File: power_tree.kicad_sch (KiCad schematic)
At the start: 4 parts, among them U3 LM1117MP-3.3

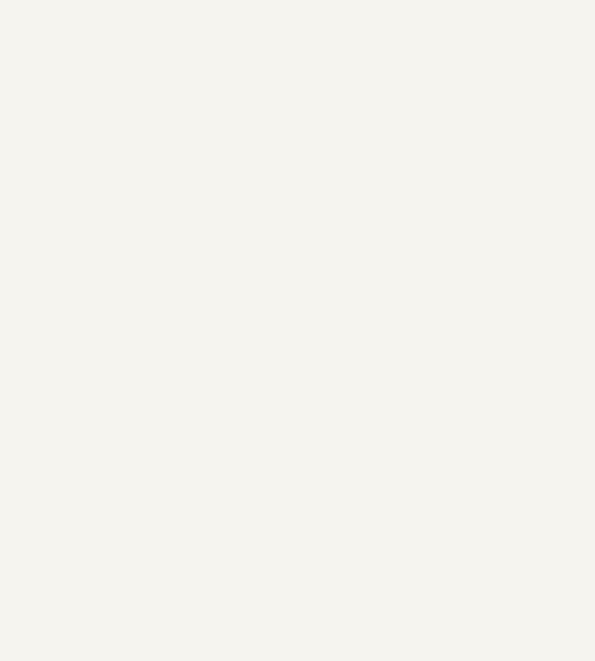
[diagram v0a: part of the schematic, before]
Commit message: feat(connector): Added USB Type-C connector for power input
This commit introduces a USB Type-C connector to the design. This connector will
serve as the primary power input for the board.

The addition of a USB Type-C connector provides a modern and versatile power
interface, offering advantages such as reversible plug orientation and the
potential for higher power delivery in the future. A separate connector
specifically for power input has also been added to provide an alternative or
dedicated power supply option.
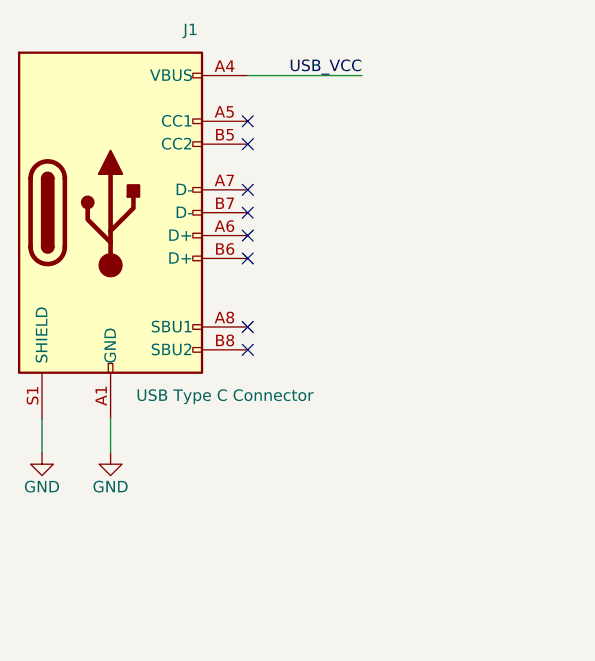
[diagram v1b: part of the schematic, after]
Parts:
- added J1: USB Type C Connector, symbol Connector:USB_C_Receptacle_USB2.0_16P
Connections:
- net GND: now also J1.A1 (GND), J1.A12 (GND), J1.B1 (GND), J1.B12 (GND), J1.S1 (SHIELD)
- net USB_VCC: now also J1.A4 (VBUS), J1.A9 (VBUS), J1.B4 (VBUS), J1.B9 (VBUS)
- no-connect marks 0 -> 8

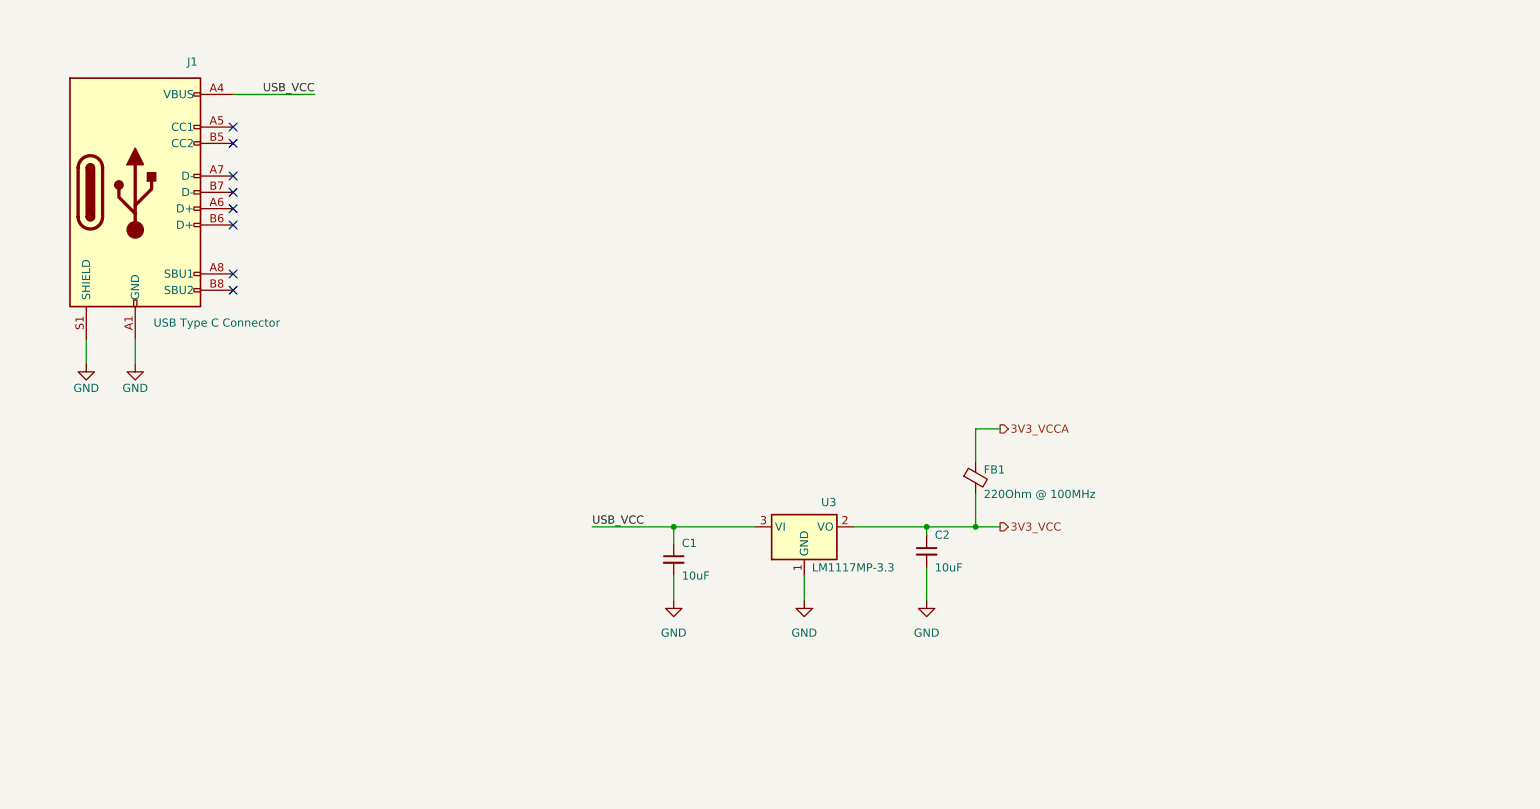
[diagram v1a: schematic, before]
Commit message: feat(usb-uart): add FT232RL USB‑UART bridge and wire RX/TX to MCU
Added the FT232RL USB‑to‑UART interface IC (FT232RL) into the schematic and powered it from the 3.3 V and 5 V rails. Exposed its TTL-level RXD and TXD pins through the hierarchical sheet and connected it to the MCU

- Placed FT232RL SSOP‑28 symbol and footprint, tied VCCIO to 3.3 V, VCC to USB_VCC, and GND to ground.
- Left legacy RS‑232 control lines (DSR#, DCD#, RI#) and CBUS pins unconnected.
- Updated hierarchy:added sheet pins on USB_UART page.

This enables USB‑serial communication between host PC and STM32F030F4Px
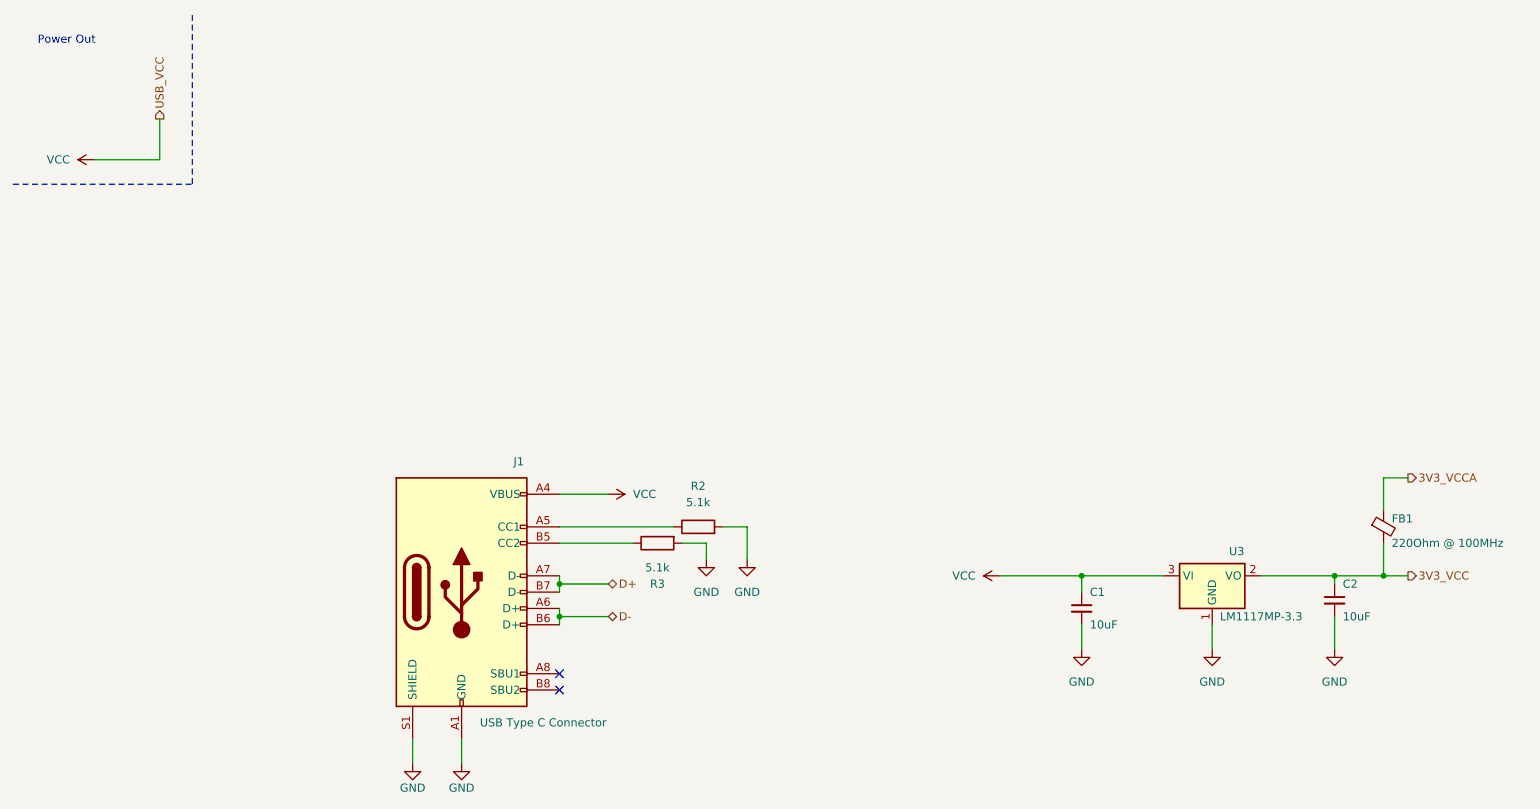
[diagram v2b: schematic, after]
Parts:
- added R2, R3: 5.1k, symbol Device:R
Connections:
- net GND: now also R2.2, R3.2
- net at J1.A5 (CC1): now also R2.1
- net D-: now reaches J1.A6 (D+)
- net D-: now also J1.B6 (D+)
- net D+: now reaches J1.A7 (D-)
- net D+: now also J1.B7 (D-)
- net at J1.B5 (CC2): now also R3.1
- net USB_VCC renamed VCC
- no-connect marks 8 -> 2
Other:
- note added: "Power Out"
- moved on the sheet: C1, C2, FB1, J1, U3

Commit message: feat(usb-uart): add FT232RL for USB-serial, update schematic and layout
Added FT232RL USB‑to‑UART interface IC, powered from 3.3 V and 5 V rails. Connected RXD and TXD to MCU via hierarchical sheet. Left RS‑232 control lines and CBUS pins unconnected. Updated hierarchy with USB_UART sheet pins.

BREAKING CHANGE: USB connector moved to USB_UART sheet; schematic wiring changed to bus-based layout. AGND now kept in separate plane using GNDA power symbol in KiCad.
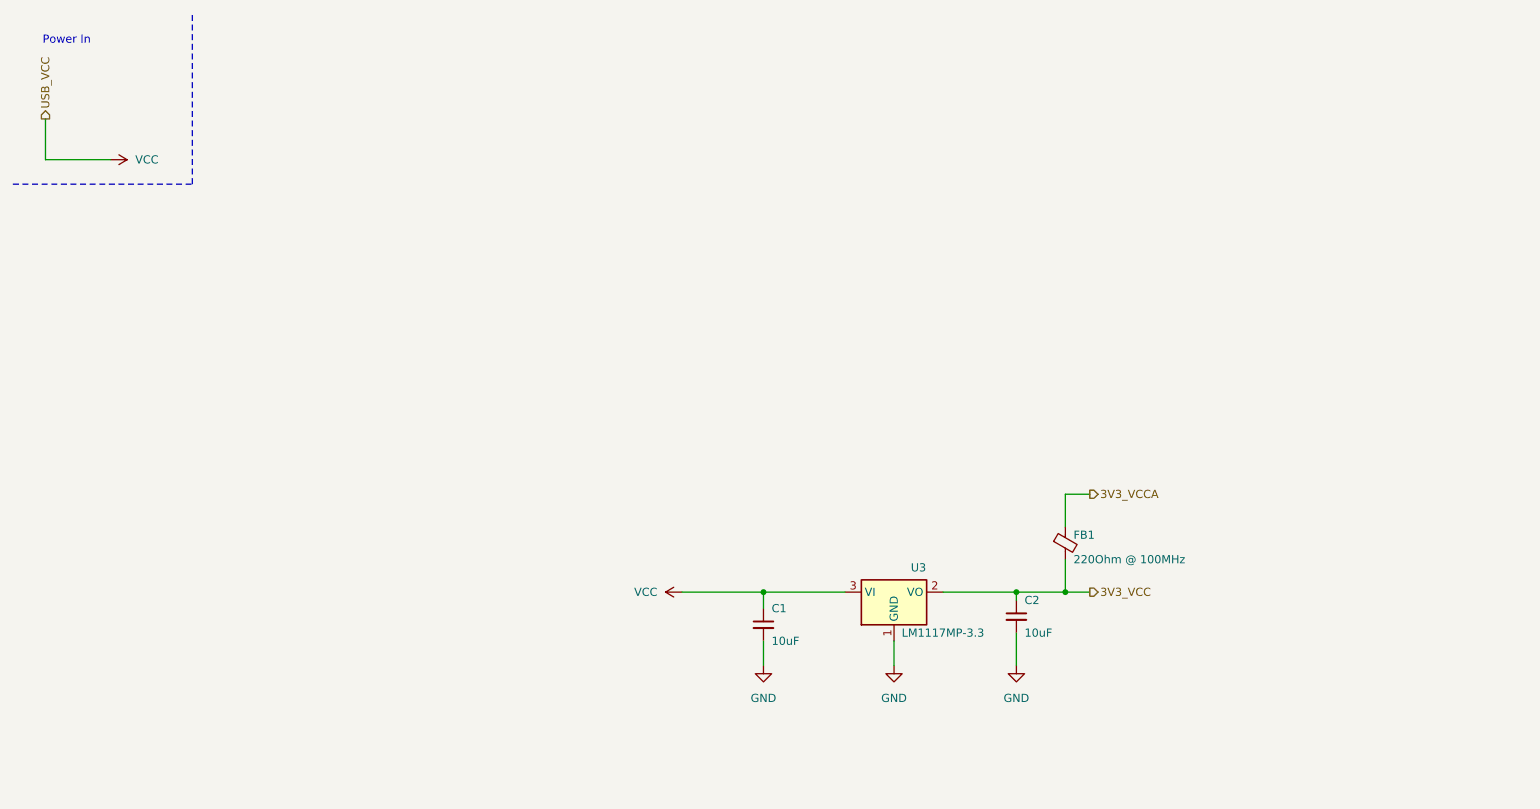
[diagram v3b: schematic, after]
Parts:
- removed J1: USB Type C Connector, symbol Connector:USB_C_Receptacle_USB2.0_16P
- removed R2, R3: 5.1k, symbol Device:R
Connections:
- no-connect marks 2 -> 0
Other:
- note added: "Power In"
- note removed: "Power Out"
- moved on the sheet: C1, C2, FB1, U3
